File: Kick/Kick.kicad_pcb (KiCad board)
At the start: 4 copper layers, 125.8 x 64 mm, 11 parts, among them J1 CN1 / J11, J2 CN2 / J12, U0 NOIP1SN1300A-QTI, U1 NOIP1SN1300A-QTI, U2 NX3L4053, U3 NX3L4053, U4 MIC5504-1.8YM5

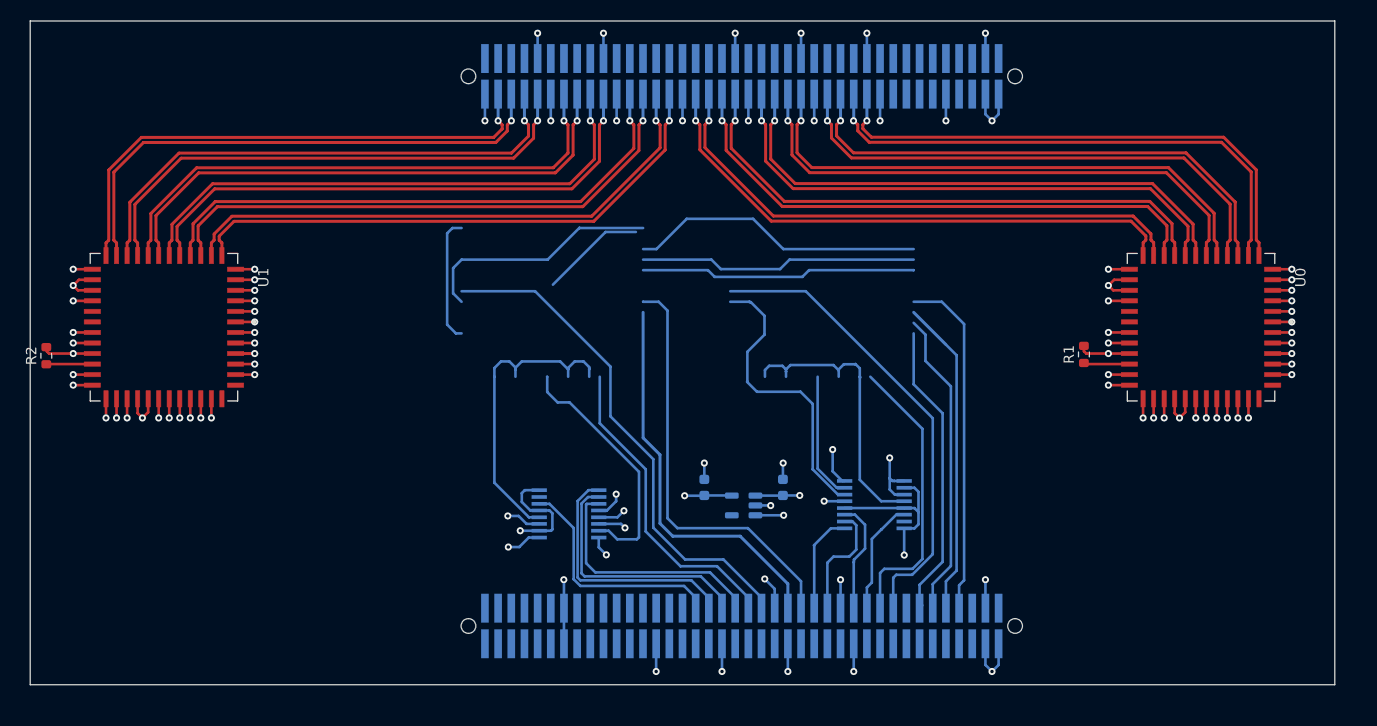
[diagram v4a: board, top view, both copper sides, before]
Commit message: finished routing and drc
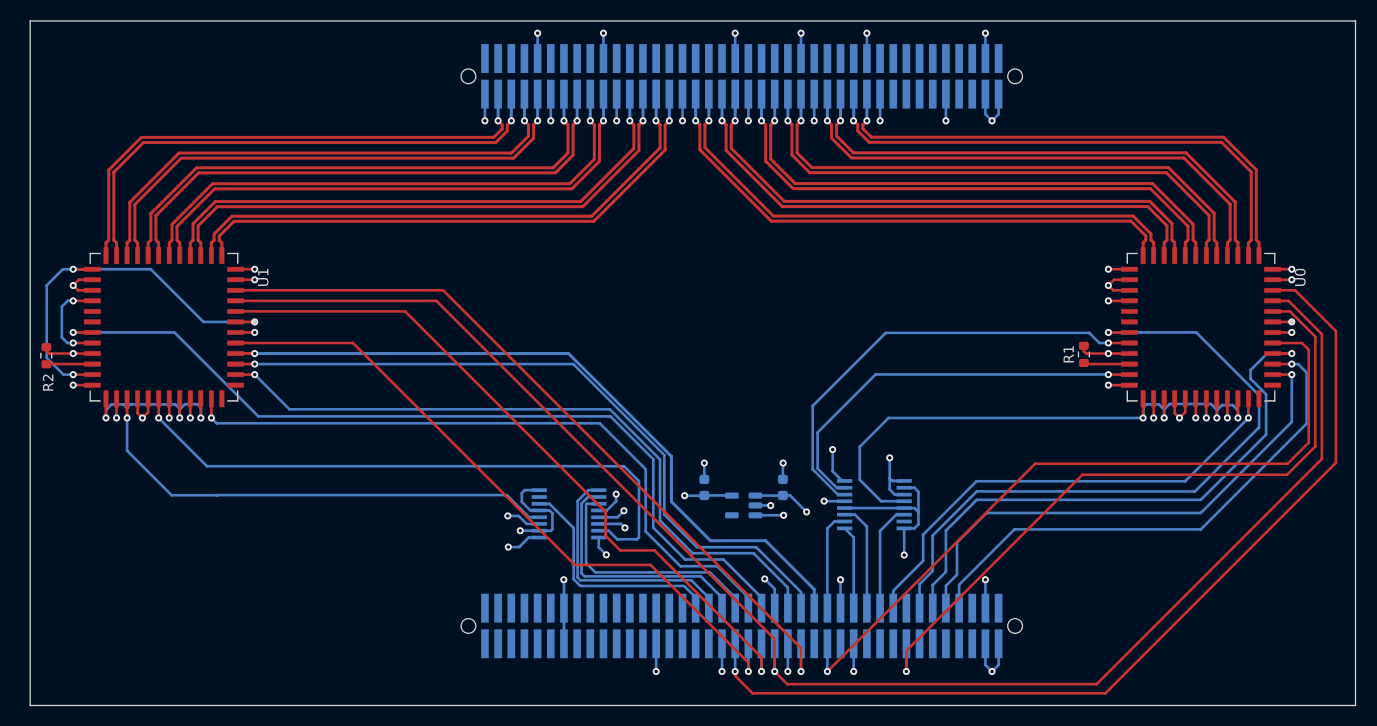
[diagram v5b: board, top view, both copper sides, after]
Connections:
- J1 pad 11: /monitor1_0 -> /resetn_0
- J1 pad 13: /monitor0_0 -> /noip_clk_0
- J1 pad 16: unconnected-(J1-Pin_16-Pad16) -> /mosi
- J1 pad 17: /noip_clk_0 -> /trigger0_0
- J1 pad 19: /trigger0_0 -> /sw_~{E}_0
- J1 pad 21: /sw_~{E}_0 -> /vdd18_toggle_0
- J1 pad 23: /vdd18_toggle_0 -> /vddpix_toggle_0
- J1 pad 28: unconnected-(J1-Pin_28-Pad28) -> /ss_0
- J1 pad 29: /vddpix_toggle_0 -> /resetn_1
- J1 pad 31: /ss_1 -> /monitor1_1
- J1 pad 32: unconnected-(J1-Pin_32-Pad32) -> /sck
- J1 pad 33: /resetn_1 -> /monitor0_1
- J1 pad 36: unconnected-(J1-Pin_36-Pad36) -> /miso
- J1 pad 38: unconnected-(J1-Pin_38-Pad38) -> /mosi
- J1 pad 40: unconnected-(J1-Pin_40-Pad40) -> /ss_1
- J1 pad 42: unconnected-(J1-Pin_42-Pad42) -> /sck
- J1 pad 7: /ss_0 -> /monitor1_0
- J1 pad 9: /resetn_0 -> /monitor0_0
- U1 pad 44: /monitor1_0 -> /monitor0_1
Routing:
- net /mosi: track 30.3 -> 153.0 mm
- net /sck: track 70.8 -> 172.9 mm
- net /miso: track 54.1 -> 151.7 mm, vias 2 -> 1
- net /monitor0_1: track 0.00 -> 67.2 mm, vias 0 -> 1
- net /monitor1_1: track 1.85 -> 68.5 mm
- net /vdd33_1: track 43.7 -> 108.9 mm
- net /ss_0: track 35.2 -> 70.9 mm
- net /vdd18_1: track 43.3 -> 78.6 mm
- net /trigger0_1: track 32.2 -> 65.3 mm
- net /noip_clk_1: track 50.7 -> 83.7 mm
- net /resetn_1: track 40.0 -> 69.6 mm
- net /vddpix_1: track 37.5 -> 66.7 mm
- net /vdd33_0: track 56.9 -> 82.2 mm
- net /resetn_0: track 32.5 -> 56.0 mm
- net /ss_1: track 42.6 -> 65.7 mm
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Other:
- board size 125.8 x 64 mm -> 127.8 x 66 mm
